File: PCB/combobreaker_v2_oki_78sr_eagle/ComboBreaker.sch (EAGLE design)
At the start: 9 parts, among them J1 7-35v

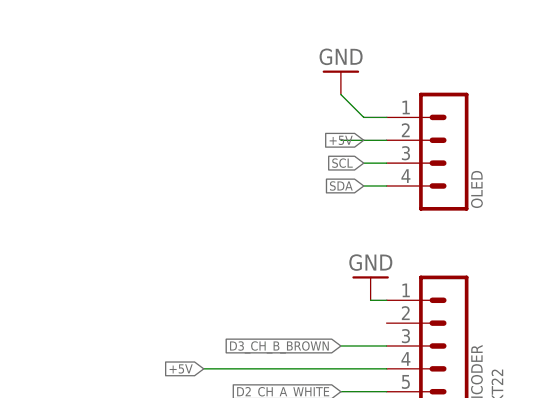
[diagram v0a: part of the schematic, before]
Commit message: Added I2C OLED Display
* Added I2C header pins for OLED display
* Reoriented JST power connector
* Rerouted VCC
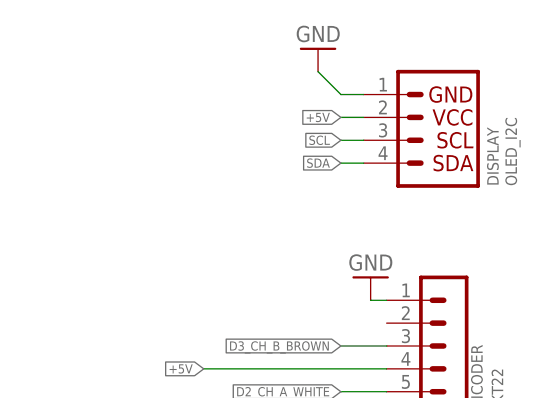
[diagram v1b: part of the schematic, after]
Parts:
- removed OLED: (no value), con-lstb:MA04-1
- added DISPLAY: OLED_I2C, SparkFun-Connectors:I2C_STANDARD
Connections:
- removed net N$4: OLED.2
- net +5V: now also DISPLAY.2
- net GND: now also DISPLAY.1; no longer OLED.1
- net SCL: now also DISPLAY.3; no longer OLED.3
- net SDA: now also DISPLAY.4; no longer OLED.4
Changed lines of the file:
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@@
 <?xml version="1.0" encoding="utf-8"?>
 <!DOCTYPE eagle SYSTEM "eagle.dtd">
-<eagle version="8.0.2">
+<eagle version="8.1.0">
 <drawing>
 <settings>
@@
 <part name="A4988" library="RepRapjr" deviceset="A4988BREAKOUT" device="" value="StepStick"/>
 <part name="J1" library="SparkFun-Connectors" deviceset="JST_2MM_MALE" device="" value="7-35v"/>
-<part name="OLED" library="con-lstb" deviceset="MA04-1" device=""/>
-<part name="GND5" library="supply1" deviceset="GND" device="" value="GND"/>
+<part name="DISPLAY" library="SparkFun-Connectors" deviceset="I2C_STANDARD" device="" value="OLED_I2C"/>
+<part name="GND9" library="supply1" deviceset="GND" device="" value="GND"/>
 </parts>
 <sheets>
@@
 <instance part="A4988" gate="G$1" x="63.5" y="38.1"/>
 <instance part="J1" gate="G$1" x="-25.4" y="86.36" rot="R90"/>
-<instance part="OLED" gate="1" x="99.06" y="111.76" smashed="yes" rot="R180">
-<attribute name="NAME" x="102.108" y="106.68" size="1.27" layer="95" font="vector" rot="R90"/>
-<attribute name="VALUE" x="104.14" y="106.68" size="1.27" layer="96" font="vector" rot="R90"/>
-</instance>
-<instance part="GND5" gate="1" x="86.36" y="121.92" rot="R180"/>
+<instance part="DISPLAY" gate="G$1" x="96.52" y="116.84" smashed="yes" rot="R180">
+<attribute name="VALUE" x="104.648" y="109.22" size="1.27" layer="96" font="vector" rot="R90" align="top-left"/>
+<attribute name="NAME" x="103.886" y="109.22" size="1.27" layer="95" font="vector" rot="R90"/>
+</instance>
+<instance part="GND9" gate="1" x="83.82" y="124.46" rot="R180"/>
 </instances>
 <busses>
@@
 </segment>
 <segment>
-<pinref part="OLED" gate="1" pin="1"/>
-<pinref part="GND5" gate="1" pin="GND"/>
-<wire x1="91.44" y1="116.84" x2="88.9" y2="116.84" width="0.1524" layer="91"/>
-<wire x1="88.9" y1="116.84" x2="86.36" y2="119.38" width="0.1524" layer="91"/>
+<pinref part="DISPLAY" gate="G$1" pin="1"/>
+<wire x1="88.9" y1="119.38" x2="86.36" y2="119.38" width="0.1524" layer="91"/>
+<pinref part="GND9" gate="1" pin="GND"/>
+<wire x1="86.36" y1="119.38" x2="83.82" y2="121.92" width="0.1524" layer="91"/>
 </segment>
 </net>
@@
 <wire x1="91.44" y1="71.12" x2="86.36" y2="71.12" width="0.1524" layer="91"/>
 <label x="86.36" y="71.12" size="1.016" layer="95" rot="R180" xref="yes"/>
-<label x="88.9" y="114.3" size="1.016" layer="95" rot="R180" xref="yes"/>
 </segment>
 <segment>
@@
 <wire x1="91.44" y1="88.9" x2="71.12" y2="88.9" width="0.1524" layer="91"/>
 <label x="71.12" y="88.9" size="1.016" layer="95" rot="R180" xref="yes"/>
+</segment>
+<segment>
+<pinref part="DISPLAY" gate="G$1" pin="2"/>
+<wire x1="88.9" y1="116.84" x2="86.36" y2="116.84" width="0.1524" layer="91"/>
+<label x="86.36" y="116.84" size="1.016" layer="95" rot="R180" xref="yes"/>
 </segment>
 </net>
@@
 </segment>
 </net>
-<net name="N$4" class="0">
-<segment>
-<pinref part="OLED" gate="1" pin="2"/>
-<wire x1="91.44" y1="114.3" x2="86.36" y2="114.3" width="0.1524" layer="91"/>
-</segment>
-</net>
 <net name="SDA" class="0">
 <segment>
@@
 </segment>
 <segment>
-<pinref part="OLED" gate="1" pin="4"/>
-<wire x1="91.44" y1="109.22" x2="88.9" y2="109.22" width="0.1524" layer="91"/>
-<label x="88.9" y="109.22" size="1.016" layer="95" rot="R180" xref="yes"/>
+<pinref part="DISPLAY" gate="G$1" pin="4"/>
+<wire x1="88.9" y1="111.76" x2="86.36" y2="111.76" width="0.1524" layer="91"/>
+<label x="86.36" y="111.76" size="1.016" layer="95" rot="R180" xref="yes"/>
 </segment>
 </net>
@@
 </segment>
 <segment>
-<pinref part="OLED" gate="1" pin="3"/>
-<label x="88.9" y="111.76" size="1.016" layer="95" rot="R180" xref="yes"/>
-<wire x1="91.44" y1="111.76" x2="88.9" y2="111.76" width="0.1524" layer="91"/>
-</segment>
-</net>
+<pinref part="DISPLAY" gate="G$1" pin="3"/>
+<wire x1="88.9" y1="114.3" x2="86.36" y2="114.3" width="0.1524" layer="91"/>
+<label x="86.36" y="114.3" size="1.016" layer="95" rot="R180" xref="yes"/>
+</segment>
+</net>

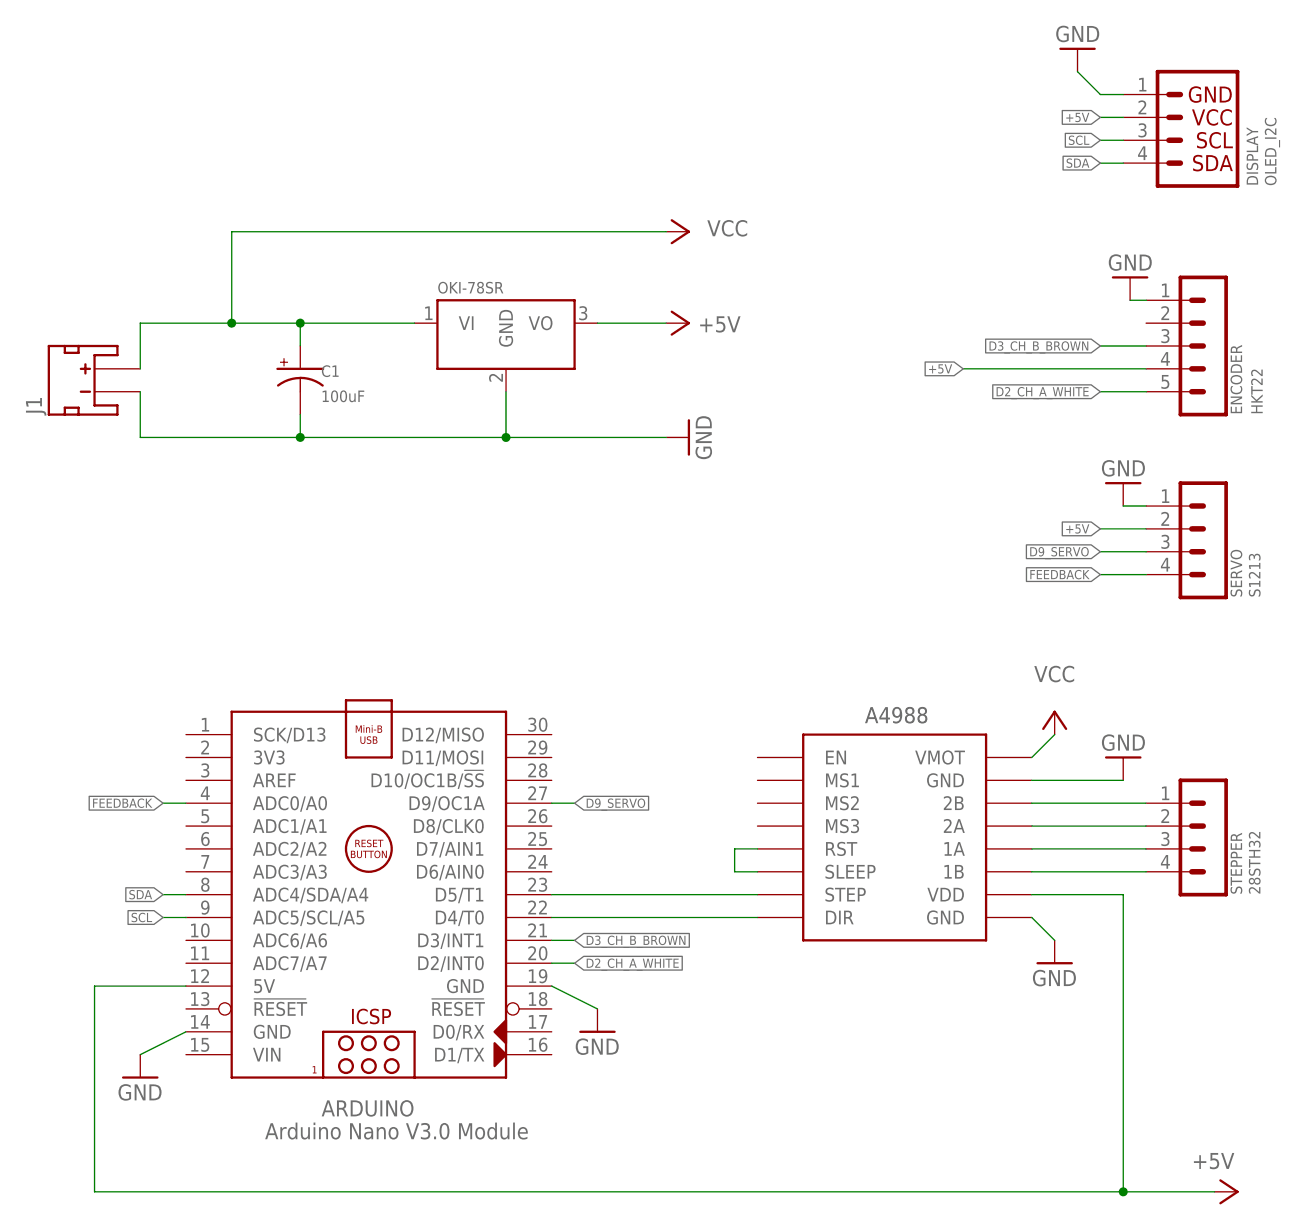
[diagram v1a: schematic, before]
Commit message: Updated v2 Eagle PCB layout
* Added standoff holes
* Added descriptions
* Added mitre to board corners
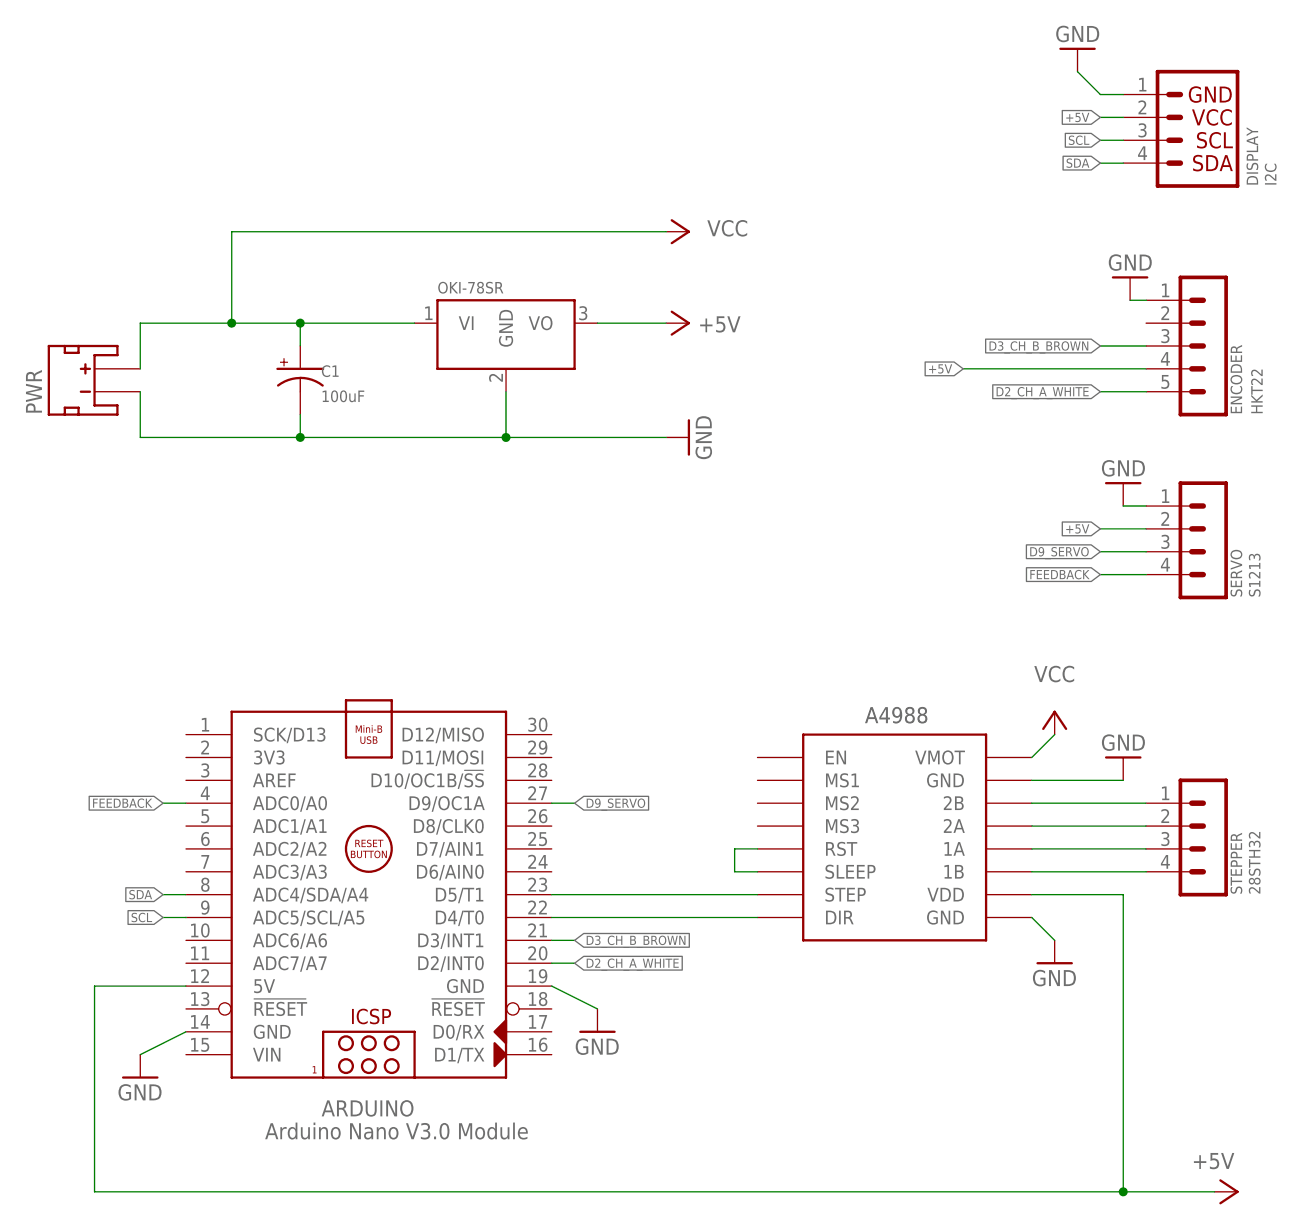
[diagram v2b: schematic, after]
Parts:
- DISPLAY: value OLED_I2C -> I2C
- renumbered J1 to PWR
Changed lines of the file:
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@@
 <part name="OKI-78SR" library="carrilib" deviceset="DCDC_OKI-78SR" device="" value="5/1.5-W36H-C"/>
 <part name="A4988" library="RepRapjr" deviceset="A4988BREAKOUT" device="" value="StepStick"/>
-<part name="J1" library="SparkFun-Connectors" deviceset="JST_2MM_MALE" device="" value="7-35v"/>
-<part name="DISPLAY" library="SparkFun-Connectors" deviceset="I2C_STANDARD" device="" value="OLED_I2C"/>
+<part name="PWR" library="SparkFun-Connectors" deviceset="JST_2MM_MALE" device="" value="7-35v"/>
+<part name="DISPLAY" library="SparkFun-Connectors" deviceset="I2C_STANDARD" device="" value="I2C"/>
 <part name="GND9" library="supply1" deviceset="GND" device="" value="GND"/>
 </parts>
@@
 </instance>
 <instance part="A4988" gate="G$1" x="63.5" y="38.1"/>
-<instance part="J1" gate="G$1" x="-25.4" y="86.36" rot="R90"/>
+<instance part="PWR" gate="G$1" x="-25.4" y="86.36" rot="R90"/>
 <instance part="DISPLAY" gate="G$1" x="96.52" y="116.84" smashed="yes" rot="R180">
 <attribute name="VALUE" x="104.648" y="109.22" size="1.27" layer="96" font="vector" rot="R90" align="top-left"/>
@@
 <junction x="-2.54" y="81.28"/>
 <pinref part="OKI-78SR" gate="G$1" pin="GND"/>
-<pinref part="J1" gate="G$1" pin="-"/>
+<pinref part="PWR" gate="G$1" pin="-"/>
 <wire x1="-20.32" y1="81.28" x2="-20.32" y2="86.36" width="0.1524" layer="91"/>
 </segment>
@@
 <junction x="-10.16" y="93.98"/>
 <pinref part="OKI-78SR" gate="G$1" pin="VI"/>
-<pinref part="J1" gate="G$1" pin="+"/>
+<pinref part="PWR" gate="G$1" pin="+"/>
 <wire x1="-20.32" y1="93.98" x2="-20.32" y2="88.9" width="0.1524" layer="91"/>
 </segment>
@@
 </sheet>
 </sheets>
+<errors>
+</errors>
 </schematic>
 </drawing>
